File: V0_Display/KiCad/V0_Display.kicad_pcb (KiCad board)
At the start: 2 copper layers, 80 x 35 mm, 28 parts, among them J1 USB_B_Micro, J2 I2C Header 1, J3 Conn_01x03, J4 Conn_01x02, J5 SWD Header, J7 USB_Header, J8 Conn_01x02, SW5 SW_SPST, SW6 SW_SPST, SW7 Rotary_Encoder_Switch, U1 AP2127K-3.3, U2 STM32F042F6Px, U3 74LVC1G17

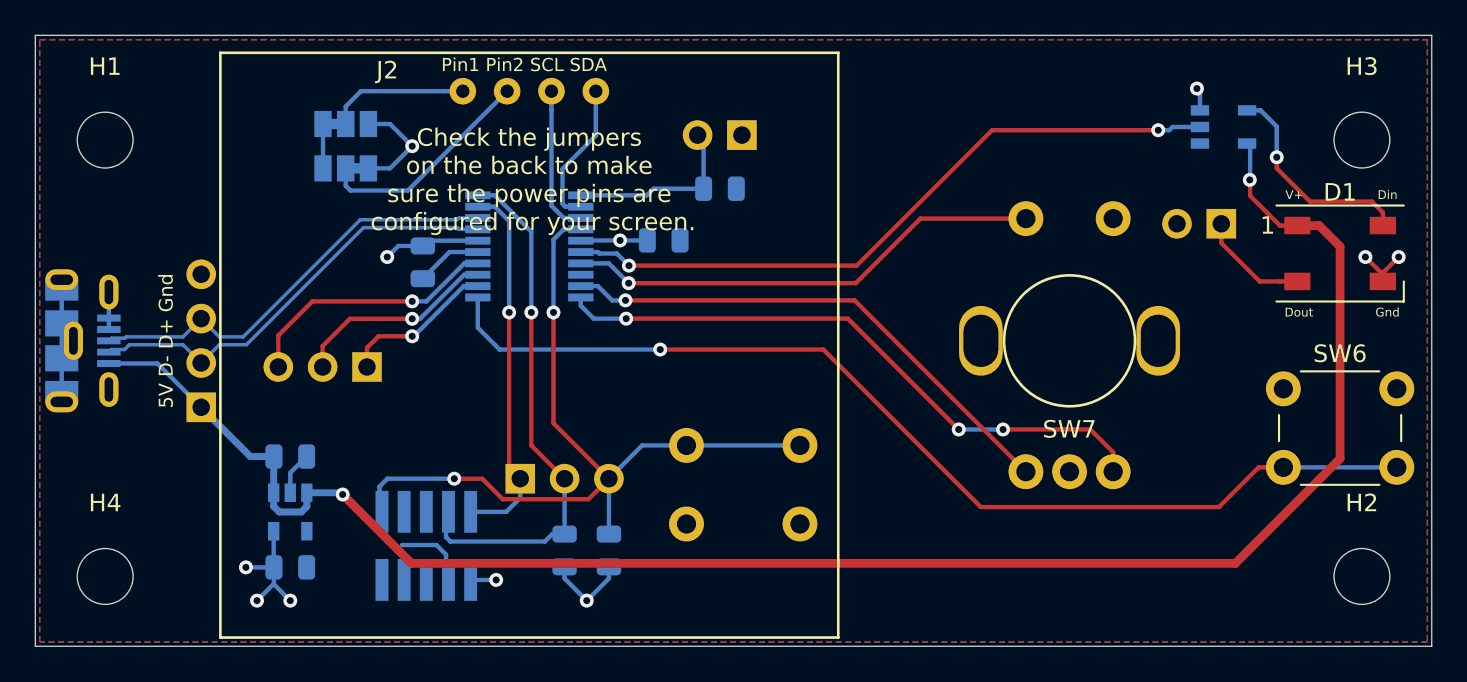
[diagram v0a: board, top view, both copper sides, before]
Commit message: Microcontroller change
Changed the STM32F042 microcontroller for an ATmega32U4, given the scarcity of the former due to the pandemic of Covid-19.
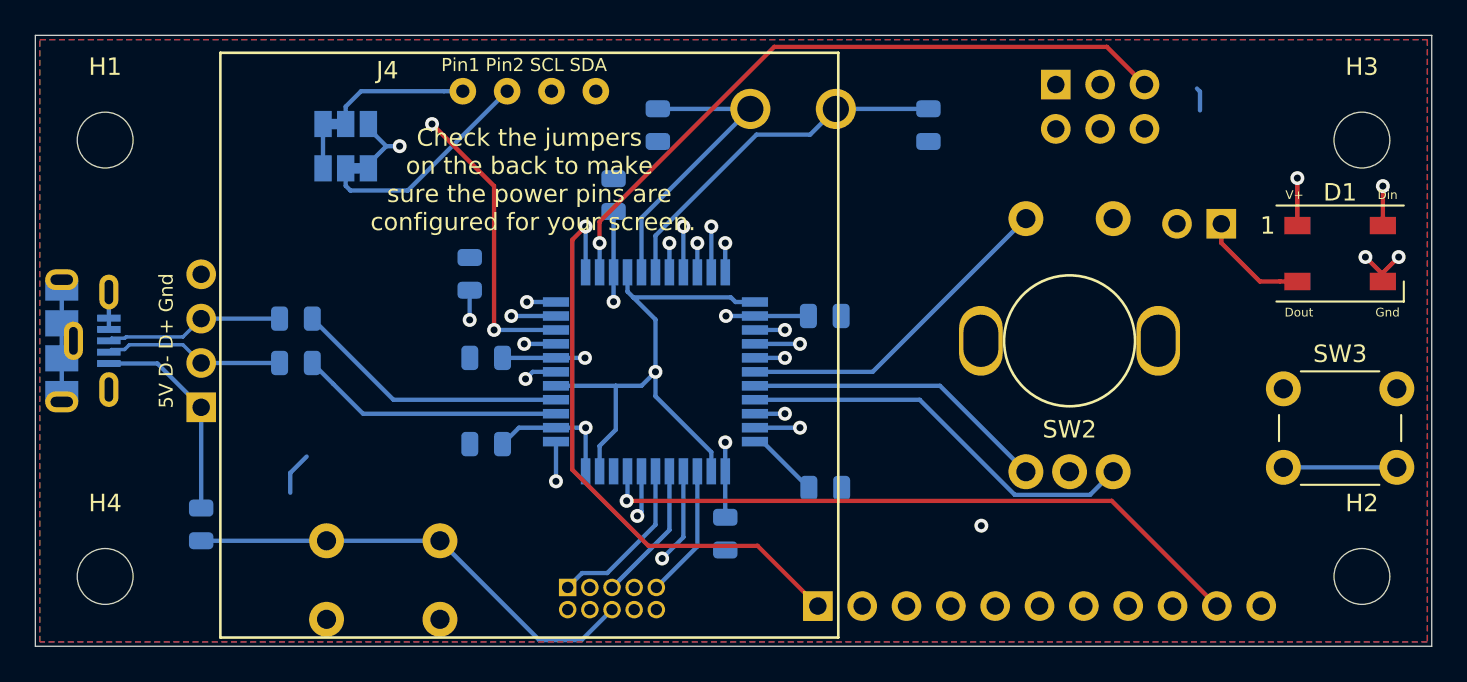
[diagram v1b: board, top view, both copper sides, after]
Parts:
- removed GPIO1: Conn_01x03, V0-Display:PinHeader_1x03_P2.54mm_Vertical
- removed the J4 at (125.7, 55.4)
- removed the J5 at (107.6, 78.9)
- removed U2: STM32F042F6Px, V0-Display:TSSOP-20_4.4x6.5mm_P0.65mm
- removed U3: 74LVC1G17, V0-Display:SOT-753
- added C5: 8pF, V0-Display:C_0805_2012Metric, B.Cu at (120.8, 54.8)
- added C6: 1µF, V0-Display:C_0805_2012Metric, B.Cu at (110.1, 63.3)
- added C7: 0.1µF, V0-Display:C_0805_2012Metric, B.Cu at (130.4, 65.7)
- added C8: 0.1µF, V0-Display:C_0805_2012Metric, B.Cu at (124.7, 78.2)
- added J6: ICSP, Pin_Headers:Pin_Header_Straight_2x03_Pitch2.54mm, B.Cu at (143.6, 52.5)
- added J7: JTAG, Pin_Headers:Pin_Header_Straight_2x05_Pitch1.27mm, B.Cu at (115.7, 81.3)
- added R4: 10K, V0-Display:R_0805_2012Metric, B.Cu at (130.4, 75.6)
- added Y1: 16MHz, Crystals:Crystal_HC50_Vertical, B.Cu at (126.1, 53.9)
- C1, C2: value 4.7uF -> 0.1µF
- C3: value 0.1uF -> 0.1µF
- C4: value 0.1uF -> 8pF
- J3: value Conn_01x03 -> Conn_01x11; footprint V0-Display:PinHeader_1x03_P2.54mm_Vertical -> Pin_Headers:Pin_Header_Straight_1x11_Pitch2.54mm
- R2, R3: value 10K -> 22R
- U1: value AP2127K-3.3 -> ATmega32U4-AU; footprint V0-Display:SOT-23-5 -> Housings_QFP:TQFP-44_10x10mm_Pitch0.8mm
- moved R2 25.4 mm to (100.1, 65.9), turned to 180 degrees
- moved R1 23.4 mm to (94.7, 77.7), turned to 270 degrees
- moved U1 22.4 mm to (120.7, 68.9), turned to 0 degrees
- moved SW1 21.3 mm to (108.4, 78.6)
- moved R3 18.8 mm to (100.1, 68.4), turned to 0 degrees
- moved J3 18.5 mm to (130.0, 82.3)
- moved C4 16.5 mm to (136.3, 54.8), turned to 270 degrees
- moved C2 16.4 mm to (111.0, 68.1)
- moved C3 11.6 mm to (118.3, 58.8), turned to 270 degrees
- moved C1 11.2 mm to (111.0, 73.1)
- renumbered J7 to J2, J2 to J4, J8 to J5, SW5 to SW1, SW7 to SW2, SW6 to SW3
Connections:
- C1 pad 1: VBUS -> GND
- C1 pad 2: GND -> VBUS
- C2 pad 1: +3V3 -> GND
- C2 pad 2: GND -> VBUS
- C3 pad 2: +3V3 -> VBUS
- C4 pad 1: +3V3 -> Net-(C4-Pad1)
- D1 pad 4: Net-(D1-Pad4) -> NeoPixel
- J3 pad 1: SWDIO -> GPIO1
- J3 pad 2: SWDCLK -> GPIO2
- J3 pad 3: ~Reset -> GPIO3
- JP1 pad 1: +3V3 -> VBUS
- JP2 pad 3: +3V3 -> VBUS
- R1 pad 1: +3V3 -> VBUS
- R2 pad 1: BOOT0 -> Net-(R2-Pad1)
- R2 pad 2: GND -> D+
- R3 pad 1: +3V3 -> D-
- R3 pad 2: SWDCLK -> Net-(R3-Pad2)
- U1 pad 1: VBUS -> NeoPixel
- U1 pad 2: GND -> VBUS
- U1 pad 3: VBUS -> Net-(R3-Pad2)
- U1 pad 4: (no net) -> Net-(R2-Pad1)
- U1 pad 5: +3V3 -> GND
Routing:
- net SCLK: track 0.00 -> 59.4 mm, vias 0 -> 2
- net MISO: track 0.00 -> 42.1 mm, vias 0 -> 1
- net MOSI: track 0.00 -> 41.9 mm, vias 0 -> 1
- net ~Reset: track 47.5 -> 89.0 mm, vias 2 -> 1
- net GPIO11: track 0.00 -> 41.5 mm, vias 0 -> 1
- net GPIO10: track 0.00 -> 38.0 mm, vias 0 -> 1
- net NeoPixel: track 39.1 -> 76.8 mm
- net VBUS: track 102.4 -> 68.3 mm, vias 2 -> 7
- net GPIO5: track 0.00 -> 31.3 mm, vias 0 -> 1
- net GPIO7: track 0.00 -> 31.0 mm, vias 0 -> 1
- net SWDCLK: track 30.6 -> 0.00 mm, vias 1 -> 0
- net GPIO9: track 0.00 -> 29.8 mm, vias 0 -> 1
- net +3V3: track 29.3 -> 0.00 mm, vias 8 -> 0
- net GPIO4: track 0.00 -> 28.5 mm, vias 0 -> 1
- net GPIO8: track 0.00 -> 27.6 mm, vias 0 -> 2
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- added copper zone on F.Cu, net GND
- added copper zone on GND, net GND
- added copper zone on VBUS, net VBUS
- removed copper zone on F.Cu, net +3V3
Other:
- copper layers 2 -> 4
- rule pad_to_mask_clearance: 0.051 -> 0
- board text added: "1"
- board text added: "2"
- board text added: "GPIO1"
- board text added: "GPIO10"
- board text added: "GPIO11"
- board text added: "GPIO2"
- board text added: "GPIO3"
- board text added: "GPIO4"
- board text added: "GPIO5"
- board text added: "GPIO6"
- board text added: "GPIO7"
- board text added: "GPIO8"
- board text added: "GPIO9"
- board text added: "JTAG"
- board text added: "T. Abraham / V. Cordeiro V0-Display - AVR edition Rev. 0.1"
- board text removed: "1 2 3 GPIO"
- board text removed: "1 9"
- board text removed: "2 10"
- board text removed: "3V3 BOOT"
- board text removed: "BOOT"
- board text removed: "Reset SWDCLK SWDIO"
- board text removed: "T. Abraham V0-Display Rev-D"
